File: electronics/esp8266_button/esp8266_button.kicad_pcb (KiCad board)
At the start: 2 copper layers, 34.3 x 50.8 mm, 23 parts, among them J1 CONN_01X03, P1 SYMBOL, Q1 Q_PMOS_GSD, Q2 Q_NMOS_GSD, SW1 SW_Push, SW2 SW_Push, SW3 SW_Push, U1 MCP1703A-3302/MB, U2 ESP-12

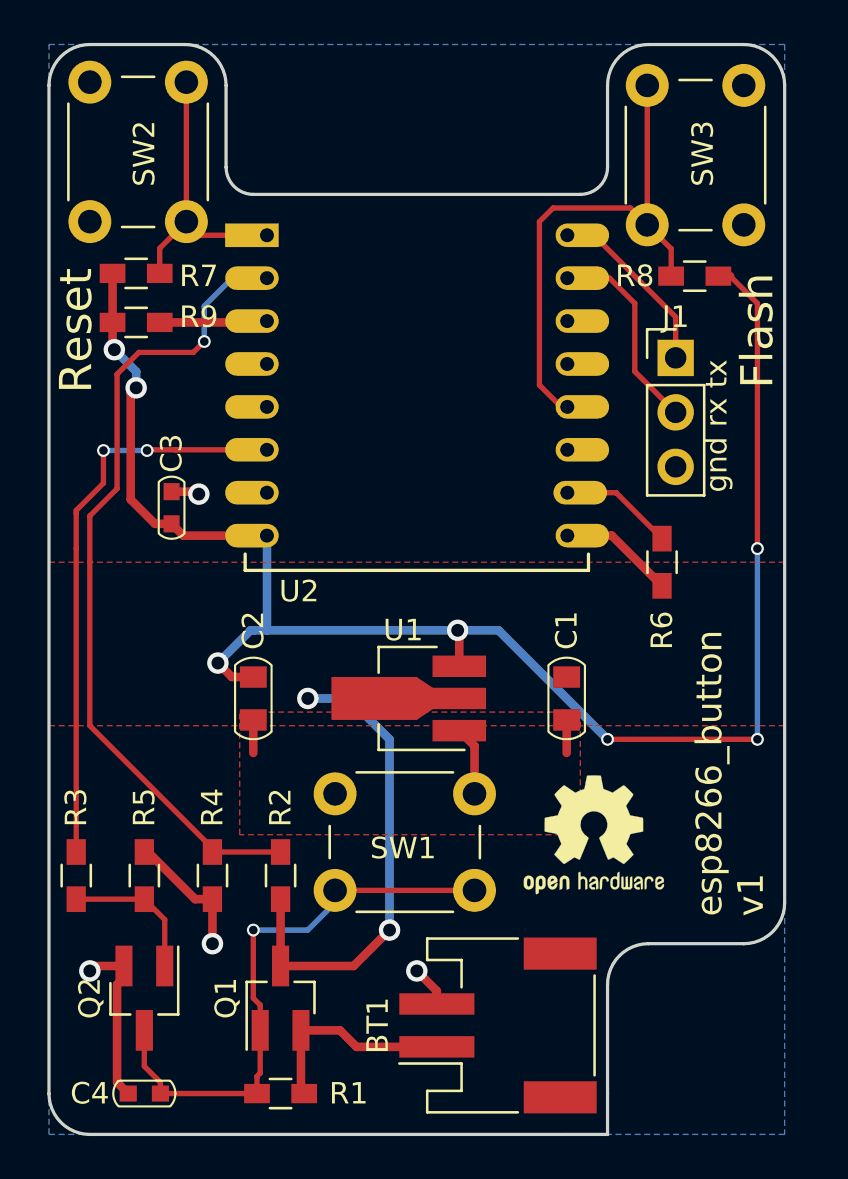
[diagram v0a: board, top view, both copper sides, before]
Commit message: Remove ground pour
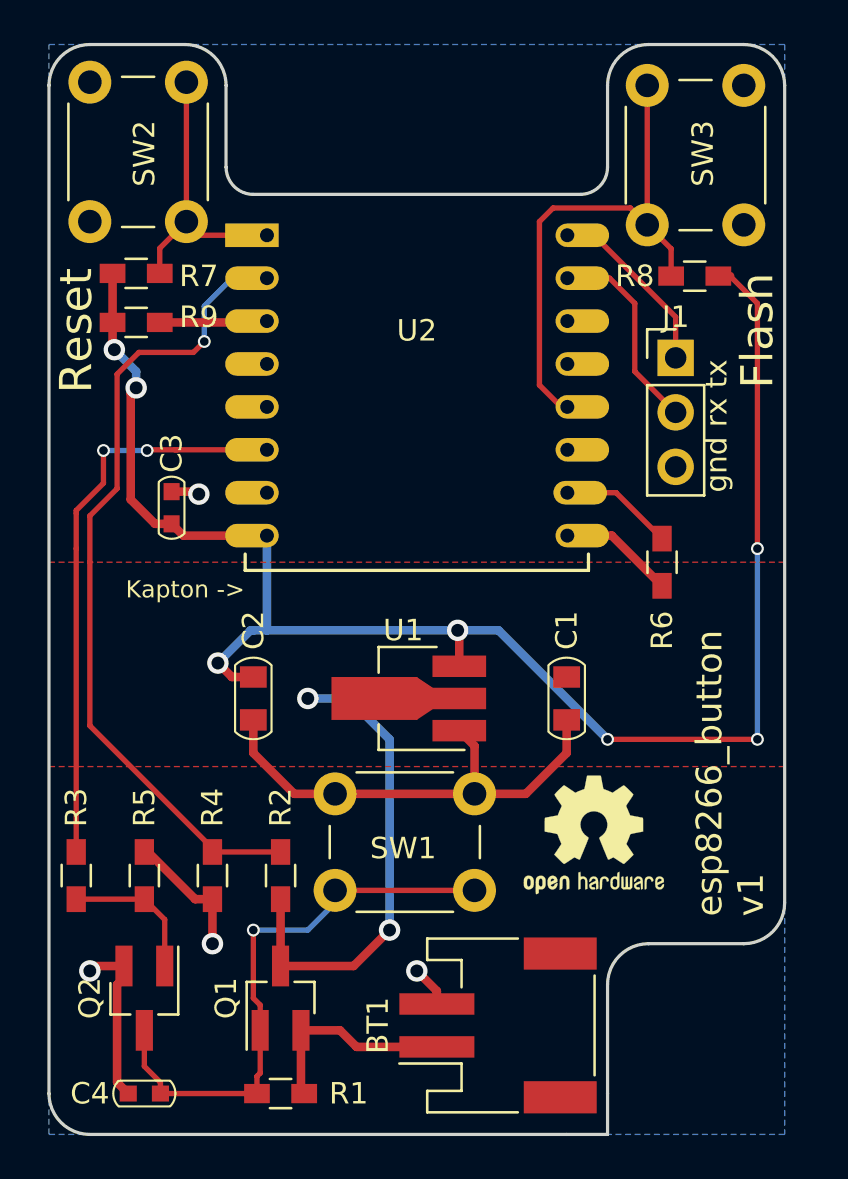
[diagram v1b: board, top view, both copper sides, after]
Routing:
- net GND: track 29.1 -> 45.3 mm
- removed copper zone on F.Cu, net GND
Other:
- board text added: "Kapton ->"
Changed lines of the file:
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@@
-(kicad_pcb (version 4) (host pcbnew 4.0.6-e0-6349~53~ubuntu14.04.1)
+(kicad_pcb (version 4) (host pcbnew 4.0.6)
   (general
     (links 50)
     (no_connects 0)
-    (area 137.084999 78.029999 171.525001 128.980001)
+    (area 135.905 78.019999 171.53 128.980001)
     (thickness 1.6)
-    (drawings 25)
-    (tracks 142)
+    (drawings 26)
+    (tracks 147)
     (zones 0)
     (modules 23)
@@
     (descr "Module, ESP-8266, ESP-12, 16 pad, SMD")
     (tags "Module ESP-8266 ESP8266")
-    (fp_text reference U2 (at 1.5 16.6) (layer F.SilkS)
+    (fp_text reference U2 (at 6.985 4.445) (layer F.SilkS)
       (effects (font (size 1 1) (thickness 0.15)))
     )
@@
       (xy -0.113933 -2.757629) (xy -0.013056 -2.757714) (xy 0 -2.757714) (xy 0.10391 -2.757652)) (layer F.SilkS) (width 0.01))
   )
+  (gr_text "Kapton ->" (at 143.51 103.505) (layer F.SilkS)
+    (effects (font (size 0.8 0.8) (thickness 0.2)))
+  )
   (gr_text "gnd rx tx" (at 168.275 95.885 90) (layer F.SilkS)
     (effects (font (size 1 1) (thickness 0.25)))
@@
   (gr_arc (start 169.545 118.11) (end 171.45 118.11) (angle 90) (layer Edge.Cuts) (width 0.15))
   (gr_arc (start 165.1 121.92) (end 163.195 121.92) (angle 90) (layer Edge.Cuts) (width 0.15))
+  (segment (start 156.995 113.03) (end 159.385 113.03) (width 0.4) (layer F.Cu) (net 1) (status 400000))
+  (segment (start 161.29 111.125) (end 161.29 109.585) (width 0.4) (layer F.Cu) (net 1))
+  (segment (start 159.385 113.03) (end 161.29 111.125) (width 0.4) (layer F.Cu) (net 1))
+  (segment (start 150.495 113.03) (end 156.995 113.03) (width 0.4) (layer F.Cu) (net 1) (status C00000))
+  (segment (start 146.685 111.125) (end 148.59 113.03) (width 0.4) (layer F.Cu) (net 1))
+  (segment (start 146.685 109.585) (end 146.685 111.125) (width 0.4) (layer F.Cu) (net 1))
+  (segment (start 148.59 113.03) (end 150.495 113.03) (width 0.4) (layer F.Cu) (net 1) (status 800000))
   (segment (start 156.995 113.03) (end 156.995 110.795) (width 0.4) (layer F.Cu) (net 1))
   (segment (start 156.995 110.795) (end 156.285 110.085) (width 0.4) (layer F.Cu) (net 1))
@@
   (segment (start 140.335 121.92) (end 140.335 126.48) (width 0.4) (layer F.Cu) (net 1))
   (segment (start 140.335 126.48) (end 140.855 127) (width 0.4) (layer F.Cu) (net 1))
-  (segment (start 146.685 109.585) (end 146.685 111.125) (width 0.4) (layer F.Cu) (net 1))
-  (segment (start 161.29 109.585) (end 161.29 111.125) (width 0.4) (layer F.Cu) (net 1))
   (segment (start 142.875 98.945) (end 144.03 98.945) (width 0.4) (layer F.Cu) (net 1))
   (via (at 144.145 99.06) (size 1) (drill 0.6) (layers F.Cu B.Cu) (net 1))
@@
   (segment (start 148.905 124.055) (end 148.905 126.85) (width 0.4) (layer F.Cu) (net 14))
   (segment (start 148.905 126.85) (end 149.055 127) (width 0.4) (layer F.Cu) (net 14))
-  (zone (net 1) (net_name GND) (layer F.Cu) (hatch edge 0.508)
-    (connect_pads (clearance 0.508))
-    (min_thickness 0.254)
-    (fill yes (arc_segments 16) (thermal_gap 0.508) (thermal_bridge_width 0.508))
-    (polygon
-      (pts
-        (xy 161.925 114.935) (xy 146.05 114.935) (xy 146.05 109.22) (xy 161.925 109.22)
-      )
-    )
-  )
   (zone (net 1) (net_name GND) (layer B.Cu) (hatch edge 0.508)
     (connect_pads (clearance 0.508))
@@
     (polygon
       (pts
-        (xy 171.45 109.855) (xy 137.16 109.855) (xy 137.16 102.235) (xy 171.45 102.235)
+        (xy 171.45 111.76) (xy 137.16 111.76) (xy 137.16 102.235) (xy 171.45 102.235)
       )
     )

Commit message: Checkpoint before bmp
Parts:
- added JP1: Button=Reset, SolderJumpers:SJ_1_NO, B.Cu at (147.3, 114.9)
- added JP2: =PowerOn, SolderJumpers:SJ_1_NO, B.Cu at (147.3, 117.5)
- added JP3: Always On, SolderJumpers:SJ_1_NO, F.Cu at (150.5, 122.6)
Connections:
- C4 pad 1: Net-(C4-Pad1) -> ~POWERON
- Q1 pad 1: Net-(C4-Pad1) -> ~POWERON
- Q2 pad 3: Net-(C4-Pad1) -> ~POWERON
- R1 pad 2: Net-(C4-Pad1) -> ~POWERON
- SW1 pad 2: Net-(C4-Pad1) -> Net-(JP1-Pad1)
- U2 pad 4: (no net) -> RESET
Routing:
- net CH_PD: track 5.02 -> 42.2 mm, vias 0 -> 1
- net Net-(C4-Pad1): track 27.0 -> 0.00 mm, vias 1 -> 0
- net ~POWERON: track 0.00 -> 17.5 mm, vias 0 -> 1
- net Net-(JP1-Pad1): track 0.00 -> 11.6 mm
- net RESET: track 13.4 -> 20.6 mm
- net /Vbat: track 9.66 -> 10.6 mm
- net BATTMON: track 22.4 -> 23.3 mm

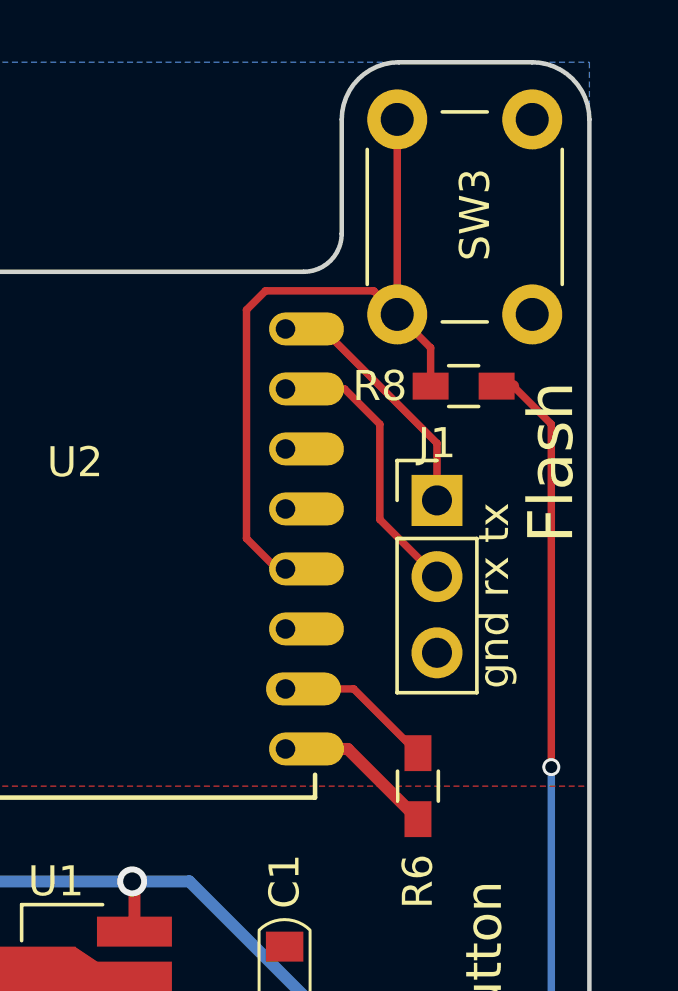
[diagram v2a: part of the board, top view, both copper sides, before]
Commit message: Fixup with bmp180
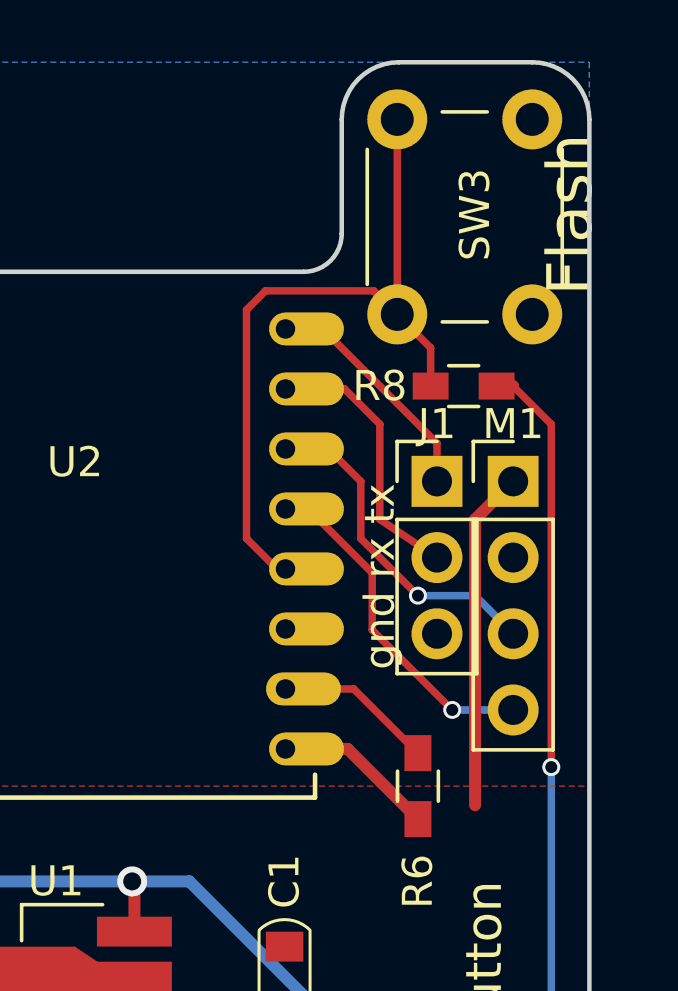
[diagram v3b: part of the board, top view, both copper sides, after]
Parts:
- added M1: BMP180_Breakout, Pin_Headers:Pin_Header_Straight_1x04_Pitch2.54mm, F.Cu at (168.9, 92.1)
- JP2: value =PowerOn -> Button=PowerOn
- moved J1 0.63 mm to (166.4, 92.1)
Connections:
- U2 pad 13: (no net) -> Net-(M1-Pad4)
- U2 pad 14: (no net) -> Net-(M1-Pad3)
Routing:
- net Net-(M1-Pad4): track 0.00 -> 11.5 mm, vias 0 -> 1
- net BATTMON: track 23.3 -> 34.6 mm
- net Net-(M1-Pad3): track 0.00 -> 11.3 mm, vias 0 -> 1
- net Net-(J1-Pad1): track 8.53 -> 7.90 mm
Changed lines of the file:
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@@
 (kicad_pcb (version 4) (host pcbnew 4.0.6)
   (general
-    (links 56)
+    (links 60)
     (no_connects 0)
     (area 137.084999 78.029999 171.525001 128.980001)
     (thickness 1.6)
     (drawings 26)
-    (tracks 169)
+    (tracks 184)
     (zones 0)
-    (modules 26)
-    (nets 16)
+    (modules 27)
+    (nets 18)
   )
   (page A4)
@@
   (net 14 ~POWERON)
   (net 15 "Net-(JP1-Pad1)")
+  (net 16 "Net-(M1-Pad4)")
+  (net 17 "Net-(M1-Pad3)")
   (net_class Default "This is the default net class."
     (clearance 0.2)
@@
     (add_net "Net-(J1-Pad2)")
     (add_net "Net-(JP1-Pad1)")
+    (add_net "Net-(M1-Pad3)")
+    (add_net "Net-(M1-Pad4)")
     (add_net "Net-(Q2-Pad1)")
     (add_net "Net-(R2-Pad2)")
@@
     (pad 12 thru_hole oval (at 14 8) (size 2.5 1.1) (drill 0.65 (offset 0.7 0)) (layers *.Cu *.Mask F.SilkS)
       (net 11 GPIO0))
-    (pad 13 thru_hole oval (at 14 6) (size 2.5 1.1) (drill 0.65 (offset 0.7 0)) (layers *.Cu *.Mask F.SilkS))
-    (pad 14 thru_hole oval (at 14 4) (size 2.5 1.1) (drill 0.65 (offset 0.7 0)) (layers *.Cu *.Mask F.SilkS))
+    (pad 13 thru_hole oval (at 14 6) (size 2.5 1.1) (drill 0.65 (offset 0.7 0)) (layers *.Cu *.Mask F.SilkS)
+      (net 16 "Net-(M1-Pad4)"))
+    (pad 14 thru_hole oval (at 14 4) (size 2.5 1.1) (drill 0.65 (offset 0.7 0)) (layers *.Cu *.Mask F.SilkS)
+      (net 17 "Net-(M1-Pad3)"))
     (pad 15 thru_hole oval (at 14 2) (size 2.5 1.1) (drill 0.65 (offset 0.7 0)) (layers *.Cu *.Mask F.SilkS)
       (net 5 "Net-(J1-Pad2)"))
@@
   )
   (module Pin_Headers:Pin_Header_Straight_1x03_Pitch2.54mm (layer F.Cu)
-    (at 166.37 92.71)
+    (at 166.37 92.075)
     (descr "Through hole straight pin header, 1x03, 2.54mm pitch, single row")
     (tags "Through hole pin header THT 1x03 2.54mm single row")
@@
       (effects (font (size 1 1) (thickness 0.15)) (justify mirror))
     )
-    (fp_text value =PowerOn (at 4.826 -1.397 180) (layer B.SilkS)
+    (fp_text value Button=PowerOn (at 4.826 -1.397 180) (layer B.SilkS)
       (effects (font (size 1 1) (thickness 0.15)) (justify mirror))
     )
@@
       (net 2 BATTMON))
   )
+  (module Pin_Headers:Pin_Header_Straight_1x04_Pitch2.54mm (layer F.Cu)
+    (at 168.91 92.075)
+    (descr "Through hole straight pin header, 1x04, 2.54mm pitch, single row")
+    (tags "Through hole pin header THT 1x04 2.54mm single row")
+    (fp_text reference M1 (at 0 -1.905) (layer F.SilkS)
+      (effects (font (size 1 1) (thickness 0.15)))
+    )
+    (fp_text value BMP180_Breakout (at 0 9.95) (layer F.Fab)
+      (effects (font (size 1 1) (thickness 0.15)))
+    )
+    (fp_line (start -0.635 -1.27) (end 1.27 -1.27) (layer F.Fab) (width 0.1))
+    (fp_line (start 1.27 -1.27) (end 1.27 8.89) (layer F.Fab) (width 0.1))
+    (fp_line (start 1.27 8.89) (end -1.27 8.89) (layer F.Fab) (width 0.1))
+    (fp_line (start -1.27 8.89) (end -1.27 -0.635) (layer F.Fab) (width 0.1))
+    (fp_line (start -1.27 -0.635) (end -0.635 -1.27) (layer F.Fab) (width 0.1))
+    (fp_line (start -1.33 8.95) (end 1.33 8.95) (layer F.SilkS) (width 0.12))
+    (fp_line (start -1.33 1.27) (end -1.33 8.95) (layer F.SilkS) (width 0.12))
+    (fp_line (start 1.33 1.27) (end 1.33 8.95) (layer F.SilkS) (width 0.12))
+    (fp_line (start -1.33 1.27) (end 1.33 1.27) (layer F.SilkS) (width 0.12))
+    (fp_line (start -1.33 0) (end -1.33 -1.33) (layer F.SilkS) (width 0.12))
+    (fp_line (start -1.33 -1.33) (end 0 -1.33) (layer F.SilkS) (width 0.12))
+    (fp_line (start -1.8 -1.8) (end -1.8 9.4) (layer F.CrtYd) (width 0.05))
+    (fp_line (start -1.8 9.4) (end 1.8 9.4) (layer F.CrtYd) (width 0.05))
+    (fp_line (start 1.8 9.4) (end 1.8 -1.8) (layer F.CrtYd) (width 0.05))
+    (fp_line (start 1.8 -1.8) (end -1.8 -1.8) (layer F.CrtYd) (width 0.05))
+    (fp_text user %R (at 0 3.81 90) (layer F.Fab)
+      (effects (font (size 1 1) (thickness 0.15)))
+    )
+    (pad 1 thru_hole rect (at 0 0) (size 1.7 1.7) (drill 1) (layers *.Cu *.Mask)
+      (net 2 BATTMON))
+    (pad 2 thru_hole oval (at 0 2.54) (size 1.7 1.7) (drill 1) (layers *.Cu *.Mask)
+      (net 1 GND))
+    (pad 3 thru_hole oval (at 0 5.08) (size 1.7 1.7) (drill 1) (layers *.Cu *.Mask)
+      (net 17 "Net-(M1-Pad3)"))
+    (pad 4 thru_hole oval (at 0 7.62) (size 1.7 1.7) (drill 1) (layers *.Cu *.Mask)
+      (net 16 "Net-(M1-Pad4)"))
+    (model ${KISYS3DMOD}/Pin_Headers.3dshapes/Pin_Header_Straight_1x04_Pitch2.54mm.wrl
+      (at (xyz 0 0 0))
+      (scale (xyz 1 1 1))
+      (rotate (xyz 0 0 0))
+    )
+  )
   (gr_text "Kapton ->" (at 143.51 103.505) (layer F.SilkS)
     (effects (font (size 0.8 0.8) (thickness 0.2)))
   )
-  (gr_text "gnd rx tx" (at 168.275 95.885 90) (layer F.SilkS)
+  (gr_text "gnd rx tx" (at 164.465 95.25 90) (layer F.SilkS)
     (effects (font (size 1 1) (thickness 0.25)))
   )
@@
     (effects (font (size 1.2 1.2) (thickness 0.3)) (justify left))
   )
-  (gr_text Flash (at 170.18 91.44 90) (layer F.SilkS)
+  (gr_text Flash (at 170.815 83.185 90) (layer F.SilkS)
     (effects (font (size 1.5 1.5) (thickness 0.3)))
   )
@@
   (via (at 144.145 99.06) (size 1) (drill 0.6) (layers F.Cu B.Cu) (net 1))
   (segment (start 144.03 98.945) (end 144.145 99.06) (width 0.4) (layer F.Cu) (net 1))
+  (segment (start 168.91 92.075) (end 167.64 93.345) (width 0.4) (layer F.Cu) (net 2))
+  (segment (start 167.64 93.345) (end 167.64 102.87) (width 0.4) (layer F.Cu) (net 2))
   (segment (start 150.495 121.055) (end 150.495 121.955) (width 0.4) (layer F.Cu) (net 2))
   (segment (start 147.955 121.055) (end 150.495 121.055) (width 0.4) (layer F.Cu) (net 2))
@@
   (segment (start 161.32 86.995) (end 162.56 86.995) (width 0.25) (layer F.Cu) (net 4))
   (segment (start 162.56 86.995) (end 166.37 90.805) (width 0.25) (layer F.Cu) (net 4))
-  (segment (start 166.37 90.805) (end 166.37 92.71) (width 0.25) (layer F.Cu) (net 4))
+  (segment (start 166.37 90.805) (end 166.37 92.075) (width 0.25) (layer F.Cu) (net 4) (status 20))
   (segment (start 161.32 88.995) (end 163.29 88.995) (width 0.25) (layer F.Cu) (net 5))
-  (segment (start 164.465 93.345) (end 166.37 95.25) (width 0.25) (layer F.Cu) (net 5))
+  (segment (start 164.465 93.345) (end 166.37 94.615) (width 0.25) (layer F.Cu) (net 5) (status 20))
   (segment (start 164.465 90.17) (end 164.465 93.345) (width 0.25) (layer F.Cu) (net 5))
   (segment (start 163.29 88.995) (end 164.465 90.17) (width 0.25) (layer F.Cu) (net 5))
@@
   (segment (start 147.92 117.475) (end 147.92 114.935) (width 0.25) (layer B.Cu) (net 15))
   (segment (start 156.995 117.53) (end 150.495 117.53) (width 0.25) (layer F.Cu) (net 15))
+  (segment (start 168.91 99.695) (end 166.878 99.695) (width 0.25) (layer B.Cu) (net 16))
+  (segment (start 164.211 95.123) (end 162.083 92.995) (width 0.25) (layer F.Cu) (net 16))
+  (segment (start 164.211 97.028) (end 164.211 95.123) (width 0.25) (layer F.Cu) (net 16))
+  (segment (start 166.878 99.695) (end 164.211 97.028) (width 0.25) (layer F.Cu) (net 16))
+  (via (at 166.878 99.695) (size 0.6) (drill 0.4) (layers F.Cu B.Cu) (net 16))
+  (segment (start 162.083 92.995) (end 161.32 92.995) (width 0.25) (layer F.Cu) (net 16))
+  (segment (start 168.91 97.155) (end 167.64 95.885) (width 0.25) (layer B.Cu) (net 17))
+  (segment (start 163.83 92.075) (end 162.75 90.995) (width 0.25) (layer F.Cu) (net 17))
+  (segment (start 163.83 93.98) (end 163.83 92.075) (width 0.25) (layer F.Cu) (net 17))
+  (segment (start 165.735 95.885) (end 163.83 93.98) (width 0.25) (layer F.Cu) (net 17))
+  (via (at 165.735 95.885) (size 0.6) (drill 0.4) (layers F.Cu B.Cu) (net 17))
+  (segment (start 167.64 95.885) (end 165.735 95.885) (width 0.25) (layer B.Cu) (net 17))
+  (segment (start 162.75 90.995) (end 161.32 90.995) (width 0.25) (layer F.Cu) (net 17))
   (zone (net 1) (net_name GND) (layer B.Cu) (hatch edge 0.508)
     (connect_pads (clearance 0.508))

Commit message: sync
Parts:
- added C4: 10u, Capacitors_SMD_Round:C_0805, F.Cu at (143.5, 108.6)
- renumbered C4 to C1, C1 to C2, C2 to C3, C3 to C5, Q2 to Q1, Q1 to Q2, R5 to R2, R7 to R4, R8 to R5, R9 to R6, R2 to R7, R4 to R8, R6 to R9
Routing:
- net BATTMON: track 34.6 -> 29.1 mm, vias 2 -> 0
- net +3V3: track 76.7 -> 71.5 mm, vias 7 -> 5
- net CH_PD: track 42.2 -> 38.7 mm
- net GND: track 45.3 -> 41.9 mm
- net GPIO0: track 24.3 -> 25.3 mm, vias 0 -> 1

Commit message: sync
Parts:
- added J2: CONN_01X08, Pin_Headers:Pin_Header_Straight_1x08_Pitch2.54mm, F.Cu at (165.7, 107.1)
- added J3: CONN_01X08, Pin_Headers:Pin_Header_Straight_1x08_Pitch2.54mm, F.Cu at (142.9, 107.1)
- C5, R4, R5, R6, R9: moved to B.Cu
- moved C4 16.0 mm to (159.5, 107.7), turned to 180 degrees
- moved R5 13.9 mm to (154.9, 95.2), turned to 0 degrees
- moved R6 13.8 mm to (154.9, 92.7), turned to 180 degrees
- moved R4 13.8 mm to (154.9, 90.2), turned to 180 degrees
- moved C3 12.9 mm to (159.5, 110.2), turned to 180 degrees
- moved R9 11.7 mm to (154.9, 97.8), turned to 180 degrees
- moved U1 10.7 mm to (163.1, 114.8), turned to 270 degrees
- moved P1 10.6 mm to (153.7, 109.2)
- moved C2 8.08 mm to (167.0, 114.3), turned to 90 degrees
- moved C5 7.00 mm to (149.6, 101.6), turned to 270 degrees
- moved M1 6.11 mm to (169.3, 98.2)
- moved J1 4.04 mm to (169.3, 89.3)
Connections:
- net Net-(J1-Pad1) renamed /TXD
- net Net-(J1-Pad2) renamed /RXD
- net Net-(M1-Pad3) renamed /GPIO5
- net Net-(M1-Pad4) renamed /GPIO4
- net Net-(R7-Pad2) renamed /ADC
- net Net-(R9-Pad1) renamed /GPIO15
- net PWR_LATCH renamed GPIO12
- U2 pad 11: (no net) -> /GPIO2
- U2 pad 5: (no net) -> /GPIO14
- U2 pad 7: (no net) -> /GPIO13
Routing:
- net +3V3: track 71.5 -> 43.9 mm, vias 5 -> 2
- net /GPIO15: track 5.58 -> 23.3 mm, vias 0 -> 3
- net BATTMON: track 29.1 -> 44.1 mm, vias 0 -> 1
- net GND: track 41.9 -> 29.1 mm, vias 4 -> 5
- net RESET: track 20.6 -> 28.2 mm, vias 0 -> 1
- net /GPIO2: track 0.00 -> 7.15 mm
- net CH_PD: track 38.7 -> 32.6 mm, vias 1 -> 4
- net /GPIO4: track 11.5 -> 17.5 mm, vias 1 -> 0
- net /GPIO13: track 0.00 -> 5.68 mm
- net GPIO0: track 25.3 -> 31.0 mm
- net /GPIO14: track 0.00 -> 5.23 mm
- net /GPIO5: track 11.3 -> 16.2 mm, vias 1 -> 0
- net /ADC: track 38.1 -> 34.3 mm
- net GPIO12: track 26.9 -> 24.9 mm, vias 2 -> 0
- net /TXD: track 7.90 -> 8.92 mm
- added copper zone on F.Cu, net +3V3
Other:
- board text added: "tx rx gnd"
- board text removed: "gnd rx tx"
